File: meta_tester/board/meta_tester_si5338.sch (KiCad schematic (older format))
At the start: 61 parts, among them J101 SMA_PCB, J102 SMA_PCB, J103 SMA_PCB, J104 SMA_PCB, J105 SMA_PCB, J106 SMA_PCB, J107 SMA_PCB, J108 SMA_PCB, P101 USB_OTG, P102 CONN_01X06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

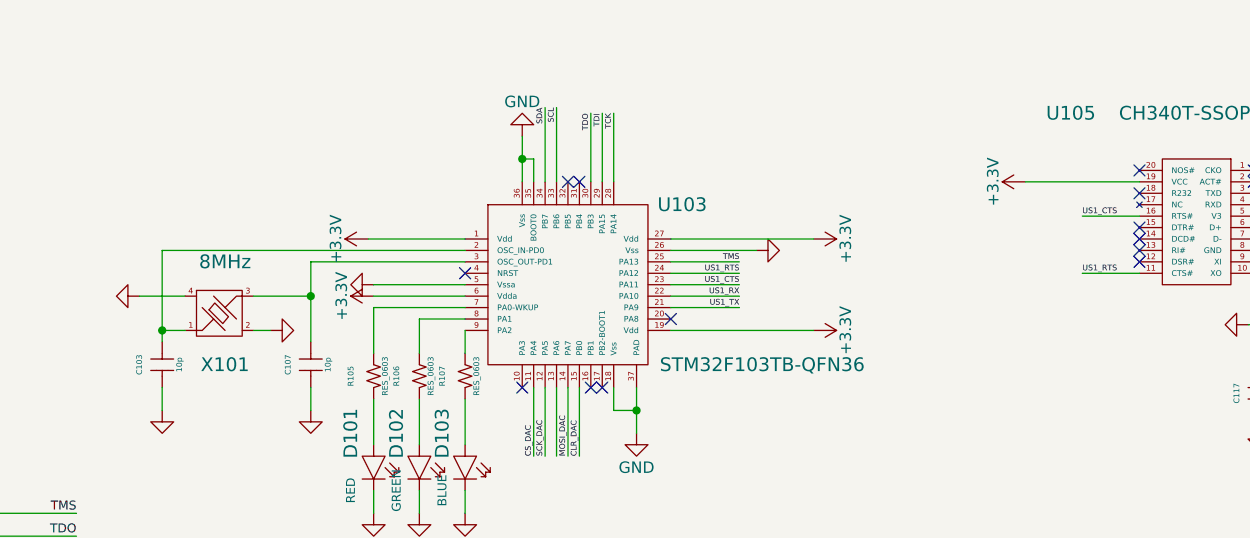
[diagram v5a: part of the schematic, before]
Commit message: starting simulation for sampling head + layout for clock board
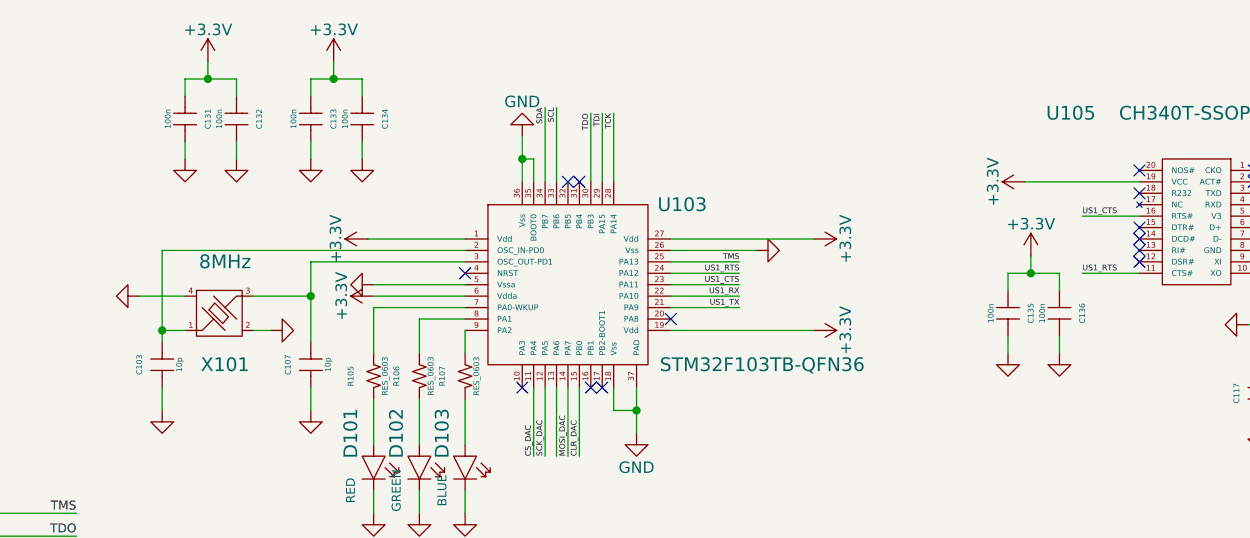
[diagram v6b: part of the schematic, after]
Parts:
- added C131, C132, C133, C134, C135, C136: 100n, General_SMD:SM0805, symbol CAP_0805
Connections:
- net +3V3: now also C131.2, C132.2, C133.2, C134.2, C135.2, C136.2
- net GND: now also C131.1, C132.1, C133.1, C134.1, C135.1, C136.1
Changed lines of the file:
@@
 	0    1    1    0
 $EndComp
+$Comp
+L CAP_0805 C135
+U 1 1 58B2449B
+P 6775 1875
+F 0 "C135" H 6775 1775 25  0000 C CNN
+F 1 "100n" H 6775 1950 25  0000 C CNN
+F 2 "General_SMD:SM0805" H 6775 1975 60  0001 C CNN
+F 3 "" H 6775 1875 60  0000 C CNN
+	1    6775 1875
+	0    -1   -1   0
+$EndComp
+$Comp
+L GND #PWR054
+U 1 1 58B244A1
+P 6775 2050
+F 0 "#PWR054" H 6775 1800 50  0001 C CNN
+F 1 "GND" H 6775 1900 50  0001 C CNN
+F 2 "" H 6775 2050 50  0000 C CNN
+F 3 "" H 6775 2050 50  0000 C CNN
+	1    6775 2050
+	1    0    0    -1
+$EndComp
+Wire Wire Line
+	6775 1975 6775 2050
+$Comp
+L CAP_0805 C136
+U 1 1 58B244A8
+P 7000 1875
+F 0 "C136" H 7000 1775 25  0000 C CNN
+F 1 "100n" H 7000 1950 25  0000 C CNN
+F 2 "General_SMD:SM0805" H 7000 1975 60  0001 C CNN
+F 3 "" H 7000 1875 60  0000 C CNN
+	1    7000 1875
+	0    -1   -1   0
+$EndComp
+$Comp
+L GND #PWR055
+U 1 1 58B244AE
+P 7000 2050
+F 0 "#PWR055" H 7000 1800 50  0001 C CNN
+F 1 "GND" H 7000 1900 50  0001 C CNN
+F 2 "" H 7000 2050 50  0000 C CNN
+F 3 "" H 7000 2050 50  0000 C CNN
+	1    7000 2050
+	1    0    0    -1
+$EndComp
+Wire Wire Line
+	7000 1975 7000 2050
+$Comp
+L +3.3V #PWR056
+U 1 1 58B244B5
+P 6875 1625
+F 0 "#PWR056" H 6875 1475 50  0001 C CNN
+F 1 "+3.3V" H 6875 1765 50  0000 C CNN
+F 2 "" H 6875 1625 50  0000 C CNN
+F 3 "" H 6875 1625 50  0000 C CNN
+	1    6875 1625
+	1    0    0    -1
+$EndComp
+Wire Wire Line
+	6875 1625 6875 1700
+Wire Wire Line
+	6775 1700 7000 1700
+Wire Wire Line
+	7000 1700 7000 1775
+Wire Wire Line
+	6775 1700 6775 1775
+Connection ~ 6875 1700
+$Comp
+L CAP_0805 C131
+U 1 1 58B245E6
+P 3175 1025
+F 0 "C131" H 3175 925 25  0000 C CNN
+F 1 "100n" H 3175 1100 25  0000 C CNN
+F 2 "General_SMD:SM0805" H 3175 1125 60  0001 C CNN
+F 3 "" H 3175 1025 60  0000 C CNN
+	1    3175 1025
+	0    -1   -1   0
+$EndComp
+$Comp
+L GND #PWR057
+U 1 1 58B245EC
+P 3175 1200
+F 0 "#PWR057" H 3175 950 50  0001 C CNN
+F 1 "GND" H 3175 1050 50  0001 C CNN
+F 2 "" H 3175 1200 50  0000 C CNN
+F 3 "" H 3175 1200 50  0000 C CNN
+	1    3175 1200
+	1    0    0    -1
+$EndComp
+Wire Wire Line
+	3175 1125 3175 1200
+$Comp
+L CAP_0805 C132
+U 1 1 58B245F3
+P 3400 1025
+F 0 "C132" H 3400 925 25  0000 C CNN
+F 1 "100n" H 3400 1100 25  0000 C CNN
+F 2 "General_SMD:SM0805" H 3400 1125 60  0001 C CNN
+F 3 "" H 3400 1025 60  0000 C CNN
+	1    3400 1025
+	0    -1   -1   0
+$EndComp
+$Comp
+L GND #PWR058
+U 1 1 58B245F9
+P 3400 1200
+F 0 "#PWR058" H 3400 950 50  0001 C CNN
+F 1 "GND" H 3400 1050 50  0001 C CNN
+F 2 "" H 3400 1200 50  0000 C CNN
+F 3 "" H 3400 1200 50  0000 C CNN
+	1    3400 1200
+	1    0    0    -1
+$EndComp
+Wire Wire Line
+	3400 1125 3400 1200
+$Comp
+L +3.3V #PWR059
+U 1 1 58B24600
+P 3275 775
+F 0 "#PWR059" H 3275 625 50  0001 C CNN
+F 1 "+3.3V" H 3275 915 50  0000 C CNN
+F 2 "" H 3275 775 50  0000 C CNN
+F 3 "" H 3275 775 50  0000 C CNN
+	1    3275 775
+	1    0    0    -1
+$EndComp
+Wire Wire Line
+	3275 775  3275 850
+Wire Wire Line
+	3175 850  3400 850
+Wire Wire Line
+	3400 850  3400 925
+Wire Wire Line
+	3175 850  3175 925
+Connection ~ 3275 850
+$Comp
+L CAP_0805 C133
+U 1 1 58B24735
+P 3725 1025
+F 0 "C133" H 3725 925 25  0000 C CNN
+F 1 "100n" H 3725 1100 25  0000 C CNN
+F 2 "General_SMD:SM0805" H 3725 1125 60  0001 C CNN
+F 3 "" H 3725 1025 60  0000 C CNN
+	1    3725 1025
+	0    -1   -1   0
+$EndComp
+$Comp
+L GND #PWR060
+U 1 1 58B2473B
+P 3725 1200
+F 0 "#PWR060" H 3725 950 50  0001 C CNN
+F 1 "GND" H 3725 1050 50  0001 C CNN
+F 2 "" H 3725 1200 50  0000 C CNN
+F 3 "" H 3725 1200 50  0000 C CNN
+	1    3725 1200
+	1    0    0    -1
+$EndComp
+Wire Wire Line
+	3725 1125 3725 1200
+$Comp
+L CAP_0805 C134
+U 1 1 58B24742
+P 3950 1025
+F 0 "C134" H 3950 925 25  0000 C CNN
+F 1 "100n" H 3950 1100 25  0000 C CNN
+F 2 "General_SMD:SM0805" H 3950 1125 60  0001 C CNN
+F 3 "" H 3950 1025 60  0000 C CNN
+	1    3950 1025
+	0    -1   -1   0
+$EndComp
+$Comp
+L GND #PWR061
+U 1 1 58B24748
+P 3950 1200
+F 0 "#PWR061" H 3950 950 50  0001 C CNN
+F 1 "GND" H 3950 1050 50  0001 C CNN
+F 2 "" H 3950 1200 50  0000 C CNN
+F 3 "" H 3950 1200 50  0000 C CNN
+	1    3950 1200
+	1    0    0    -1
+$EndComp
+Wire Wire Line
+	3950 1125 3950 1200
+$Comp
+L +3.3V #PWR062
+U 1 1 58B2474F
+P 3825 775
+F 0 "#PWR062" H 3825 625 50  0001 C CNN
+F 1 "+3.3V" H 3825 915 50  0000 C CNN
+F 2 "" H 3825 775 50  0000 C CNN
+F 3 "" H 3825 775 50  0000 C CNN
+	1    3825 775
+	1    0    0    -1
+$EndComp
+Wire Wire Line
+	3825 775  3825 850
+Wire Wire Line
+	3725 850  3950 850
+Wire Wire Line
+	3950 850  3950 925
+Wire Wire Line
+	3725 850  3725 925
+Connection ~ 3825 850
 $EndSCHEMATC

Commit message: blabla
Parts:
- U106: footprint SOT:SOT-236-095mm -> SOT:SOT23-5
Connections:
- net DAC2: now also U101.6 (OUTD), U104.9 (INA+); no longer U101.5 (OUTC), U104.8 (INB+)
- net DAC3: now also U101.5 (OUTC), U104.8 (INB+); no longer U101.6 (OUTD), U104.9 (INA+)
- net 5V01: now reaches C123.1, L103.2, U106.1 (Vin), U106.3 (EN)
- net L_N: now reaches C128.2, U106.4 (NR)
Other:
- moved on the sheet: C128
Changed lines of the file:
@@
 Text Label 1675 5025 0    25   ~ 0
 CLR_DAC
-Text Label 3595 4520 0    25   ~ 0
+Text Label 3780 4520 0    25   ~ 0
 DAC0
-Text Label 3580 5150 0    25   ~ 0
+Text Label 3770 5150 0    25   ~ 0
 DAC1
-Text Label 3580 5560 0    25   ~ 0
+Text Label 3695 5660 0    25   ~ 0
 DAC2
-Text Label 3580 5660 0    25   ~ 0
+Text Label 3600 5560 0    25   ~ 0
 DAC3
 $Comp
@@
 F 0 "U106" H 10125 1700 60  0000 C CNN
 F 1 "REG113-XX-SOT23" H 10125 1200 60  0000 C CNN
-F 2 "SOT:SOT-236-095mm" H 10125 1450 60  0001 C CNN
+F 2 "SOT:SOT23-5" H 10125 1450 60  0001 C CNN
 F 3 "" H 10125 1450 60  0000 C CNN
 	1    10125 1450
@@
 L CAP_0603 C128
 U 1 1 58AFC7CB
-P 10575 1550
-F 0 "C128" H 10575 1450 25  0000 C CNN
-F 1 "10n" H 10575 1625 25  0000 C CNN
-F 2 "General_SMD:SM0603" H 10575 1650 60  0001 C CNN
-F 3 "" H 10575 1550 60  0000 C CNN
-	1    10575 1550
+P 10725 1950
+F 0 "C128" H 10725 1850 25  0000 C CNN
+F 1 "10n" H 10725 2025 25  0000 C CNN
+F 2 "General_SMD:SM0603" H 10725 2050 60  0001 C CNN
+F 3 "" H 10725 1950 60  0000 C CNN
+	1    10725 1950
 	-1   0    0    1
 $EndComp
@@
 L GND #PWR025
 U 1 1 58AFC903
-P 10775 1550
-F 0 "#PWR025" H 10775 1300 50  0001 C CNN
-F 1 "GND" H 10775 1400 50  0001 C CNN
-F 2 "" H 10775 1550 50  0000 C CNN
-F 3 "" H 10775 1550 50  0000 C CNN
-	1    10775 1550
+P 10925 1950
+F 0 "#PWR025" H 10925 1700 50  0001 C CNN
+F 1 "GND" H 10925 1800 50  0001 C CNN
+F 2 "" H 10925 1950 50  0000 C CNN
+F 3 "" H 10925 1950 50  0000 C CNN
+	1    10925 1950
 	0    -1   -1   0
 $EndComp
@@
 	10375 1550 10475 1550
 Wire Wire Line
-	10775 1550 10675 1550
+	10925 1950 10825 1950
 $Comp
 L CAP_0805 C123
@@
 	3725 850  3725 925
 Connection ~ 3825 850
+Text Label 9600 1350 0    39   ~ 0
+5V01
+Wire Wire Line
+	10625 1950 10475 1950
+Wire Wire Line
+	10475 1950 10475 1550
+Text Label 10500 1950 0    39   ~ 0
+L_N
 $EndSCHEMATC

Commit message: almost finished pcb
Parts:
- J101, J102, J103, J104, J105, J106, J107, J108: footprint Connectors_RF:Border_Antenna -> Connectors_RF:SMA_AMP_132322
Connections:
- net 5338_INT: now also U103.13 (PA6)
- net DAC0: now also U102.9 (INA+); no longer U102.8 (INB+)
- net DAC1: now also U102.8 (INB+); no longer U102.9 (INA+)
- net DAC2: now also U104.8 (INB+); no longer U104.9 (INA+)
- net DAC3: now also U104.9 (INA+); no longer U104.8 (INB+)
- net VddO0: now also U104.10 (INA-), U104.16 (OutA); no longer U102.2 (OutB), U102.7 (INB-)
- net VddO1: now also U104.2 (OutB), U104.7 (INB-); no longer U102.10 (INA-), U102.16 (OutA)
- net VddO2: now also U102.10 (INA-), U102.16 (OutA); no longer U104.2 (OutB), U104.7 (INB-)
- net VddO3: now also U102.2 (OutB), U102.7 (INB-); no longer U104.10 (INA-), U104.16 (OutA)
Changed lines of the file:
@@
 	5790 4800 5790 3995
 Wire Wire Line
-	5540 3995 7640 3995
-Wire Wire Line
 	5840 5300 5840 5580
 Wire Wire Line
@@
 Wire Wire Line
 	6350 5580 6350 4095
-Wire Wire Line
-	6350 4095 7640 4095
 Wire Wire Line
 	5840 4800 5840 4600
@@
 Connection ~ 4385 4535
 Wire Wire Line
-	4260 3795 7640 3795
-Wire Wire Line
-	5070 3895 7640 3895
-Wire Wire Line
 	4510 3795 4510 4595
 Wire Wire Line
 	5070 5375 5070 3895
-Text Label 6655 3795 0    39   ~ 0
+Text Label 6630 4095 0    39   ~ 0
 VddO0
-Text Label 6655 3895 0    39   ~ 0
+Text Label 6600 3995 0    39   ~ 0
 VddO1
-Text Label 6655 3995 0    39   ~ 0
+Text Label 6835 3895 0    39   ~ 0
 VddO2
-Text Label 6655 4095 0    39   ~ 0
+Text Label 6830 3795 0    39   ~ 0
 VddO3
 $Comp
@@
 Connection ~ 4510 3795
 Wire Wire Line
-	2550 4825 3420 4825
-Wire Wire Line
-	3420 4825 3420 4520
-Wire Wire Line
-	3420 4520 4210 4520
-Wire Wire Line
-	4210 4520 4210 4595
-Wire Wire Line
-	2550 4875 3420 4875
-Wire Wire Line
-	3420 4875 3420 5150
-Wire Wire Line
-	3420 5150 4210 5150
-Wire Wire Line
-	4210 5150 4210 5095
+	2550 4825 3820 4825
+Wire Wire Line
+	2550 4875 4025 4875
 Wire Wire Line
 	2550 4925 3215 4925
@@
 	3215 4925 3215 5560
 Wire Wire Line
-	3215 5560 5185 5560
-Wire Wire Line
-	5185 5560 5185 4690
+	3215 5560 5490 5560
 Wire Wire Line
 	5185 4690 5490 4690
@@
 Wire Wire Line
 	3115 4975 3115 5660
-Wire Wire Line
-	3115 5660 5490 5660
-Wire Wire Line
-	5490 5660 5490 5300
 $Comp
 L GND #PWR05
@@
 Text Label 1675 5025 0    25   ~ 0
 CLR_DAC
-Text Label 3780 4520 0    25   ~ 0
+Text Label 3290 4825 0    25   ~ 0
 DAC0
-Text Label 3770 5150 0    25   ~ 0
+Text Label 3300 4875 0    25   ~ 0
 DAC1
 Text Label 3695 5660 0    25   ~ 0
@@
 F 0 "J101" H 10750 2800 60  0000 C CNN
 F 1 "SMA_PCB" H 10925 3100 60  0001 C CNN
-F 2 "Connectors_RF:Border_Antenna" H 10925 2900 25  0001 C CNN
+F 2 "Connectors_RF:SMA_AMP_132322" H 10925 2900 25  0001 C CNN
 F 3 "" H 10925 2900 25  0001 C CNN
 	1    10925 2900
@@
 F 0 "J102" H 10750 3000 60  0000 C CNN
 F 1 "SMA_PCB" H 10925 3300 60  0001 C CNN
-F 2 "Connectors_RF:Border_Antenna" H 10925 3100 25  0001 C CNN
+F 2 "Connectors_RF:SMA_AMP_132322" H 10925 3100 25  0001 C CNN
 F 3 "" H 10925 3100 25  0001 C CNN
 	1    10925 3100
@@
 F 0 "J103" H 10750 3300 60  0000 C CNN
 F 1 "SMA_PCB" H 10925 3600 60  0001 C CNN
-F 2 "Connectors_RF:Border_Antenna" H 10925 3400 25  0001 C CNN
+F 2 "Connectors_RF:SMA_AMP_132322" H 10925 3400 25  0001 C CNN
 F 3 "" H 10925 3400 25  0001 C CNN
 	1    10925 3400
@@
 F 0 "J104" H 10750 3500 60  0000 C CNN
 F 1 "SMA_PCB" H 10925 3800 60  0001 C CNN
-F 2 "Connectors_RF:Border_Antenna" H 10925 3600 25  0001 C CNN
+F 2 "Connectors_RF:SMA_AMP_132322" H 10925 3600 25  0001 C CNN
 F 3 "" H 10925 3600 25  0001 C CNN
 	1    10925 3600
@@
 F 0 "J105" H 10750 3775 60  0000 C CNN
 F 1 "SMA_PCB" H 10925 4075 60  0001 C CNN
-F 2 "Connectors_RF:Border_Antenna" H 10925 3875 25  0001 C CNN
+F 2 "Connectors_RF:SMA_AMP_132322" H 10925 3875 25  0001 C CNN
 F 3 "" H 10925 3875 25  0001 C CNN
 	1    10925 3875
@@
 F 0 "J106" H 10750 3975 60  0000 C CNN
 F 1 "SMA_PCB" H 10925 4275 60  0001 C CNN
-F 2 "Connectors_RF:Border_Antenna" H 10925 4075 25  0001 C CNN
+F 2 "Connectors_RF:SMA_AMP_132322" H 10925 4075 25  0001 C CNN
 F 3 "" H 10925 4075 25  0001 C CNN
 	1    10925 4075
@@
 F 0 "J107" H 10750 4275 60  0000 C CNN
 F 1 "SMA_PCB" H 10925 4575 60  0001 C CNN
-F 2 "Connectors_RF:Border_Antenna" H 10925 4375 25  0001 C CNN
+F 2 "Connectors_RF:SMA_AMP_132322" H 10925 4375 25  0001 C CNN
 F 3 "" H 10925 4375 25  0001 C CNN
 	1    10925 4375
@@
 F 0 "J108" H 10750 4475 60  0000 C CNN
 F 1 "SMA_PCB" H 10925 4775 60  0001 C CNN
-F 2 "Connectors_RF:Border_Antenna" H 10925 4575 25  0001 C CNN
+F 2 "Connectors_RF:SMA_AMP_132322" H 10925 4575 25  0001 C CNN
 F 3 "" H 10925 4575 25  0001 C CNN
 	1    10925 4575
@@
 Text Label 10500 1950 0    39   ~ 0
 L_N
+Wire Wire Line
+	3820 4825 3820 5150
+Wire Wire Line
+	3820 5150 4210 5150
+Wire Wire Line
+	4210 5150 4210 5095
+Wire Wire Line
+	4025 4875 4025 4565
+Wire Wire Line
+	4025 4565 4210 4565
+Wire Wire Line
+	4210 4565 4210 4595
+Wire Wire Line
+	5490 5560 5490 5300
+Wire Wire Line
+	5185 4690 5185 5660
+Wire Wire Line
+	5185 5660 3115 5660
+Text Label 4800 2500 1    25   ~ 0
+5338_INT
+Wire Wire Line
+	5070 3895 7160 3895
+Wire Wire Line
+	7160 3895 7160 3995
+Wire Wire Line
+	7160 3995 7640 3995
+Wire Wire Line
+	4260 3795 7365 3795
+Wire Wire Line
+	7365 3795 7365 4095
+Wire Wire Line
+	7365 4095 7640 4095
+Wire Wire Line
+	5540 3995 7060 3995
+Wire Wire Line
+	7060 3995 7060 3935
+Wire Wire Line
+	7060 3935 7545 3935
+Wire Wire Line
+	7545 3935 7545 3895
+Wire Wire Line
+	7545 3895 7640 3895
+Wire Wire Line
+	6350 4095 7300 4095
+Wire Wire Line
+	7300 4095 7300 3835
+Wire Wire Line
+	7300 3835 7460 3835
+Wire Wire Line
+	7460 3835 7460 3795
+Wire Wire Line
+	7460 3795 7640 3795
 $EndSCHEMATC
